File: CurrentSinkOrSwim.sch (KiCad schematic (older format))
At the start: 0 parts

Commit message: made a schematic
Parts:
- added C? (x3): C, ~, symbol C
- added P?: CONN_2, symbol CONN_2
- added Q?: BUK9575, ~, symbol MOSFET_N
- added R?: 0.1, ~, symbol R
- added R?: 27K, ~, symbol R
- added R?: 26.6K, ~, symbol R
- added R?: 0, ~, symbol R
- added R? (x2): R, ~, symbol R
- added U?: LM2931D-R, ~, symbol LM2931D-R
- added U? (x2): OP275, symbol OP275
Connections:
- net labels added: 2.7V, GND
- wire segments 0 -> 41

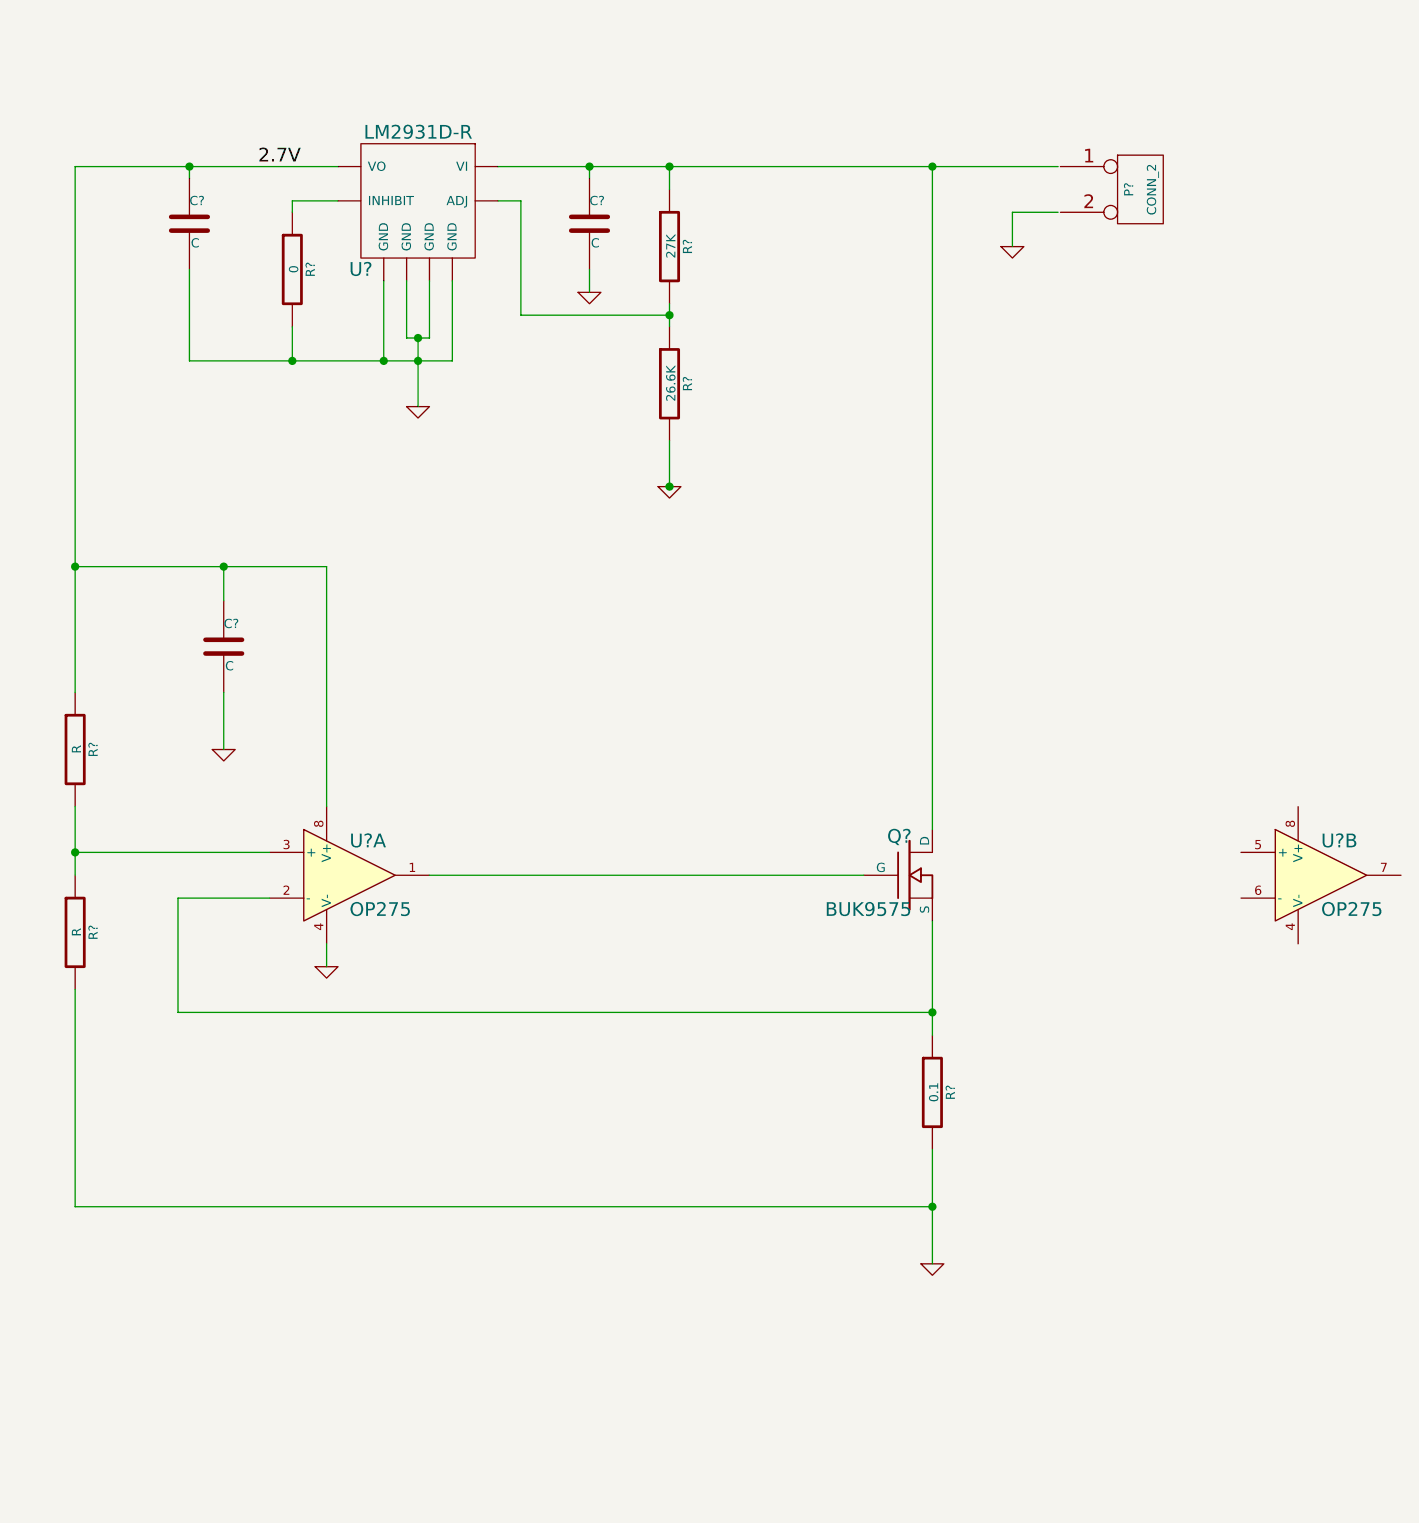
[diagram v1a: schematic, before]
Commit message: Updating the schematic
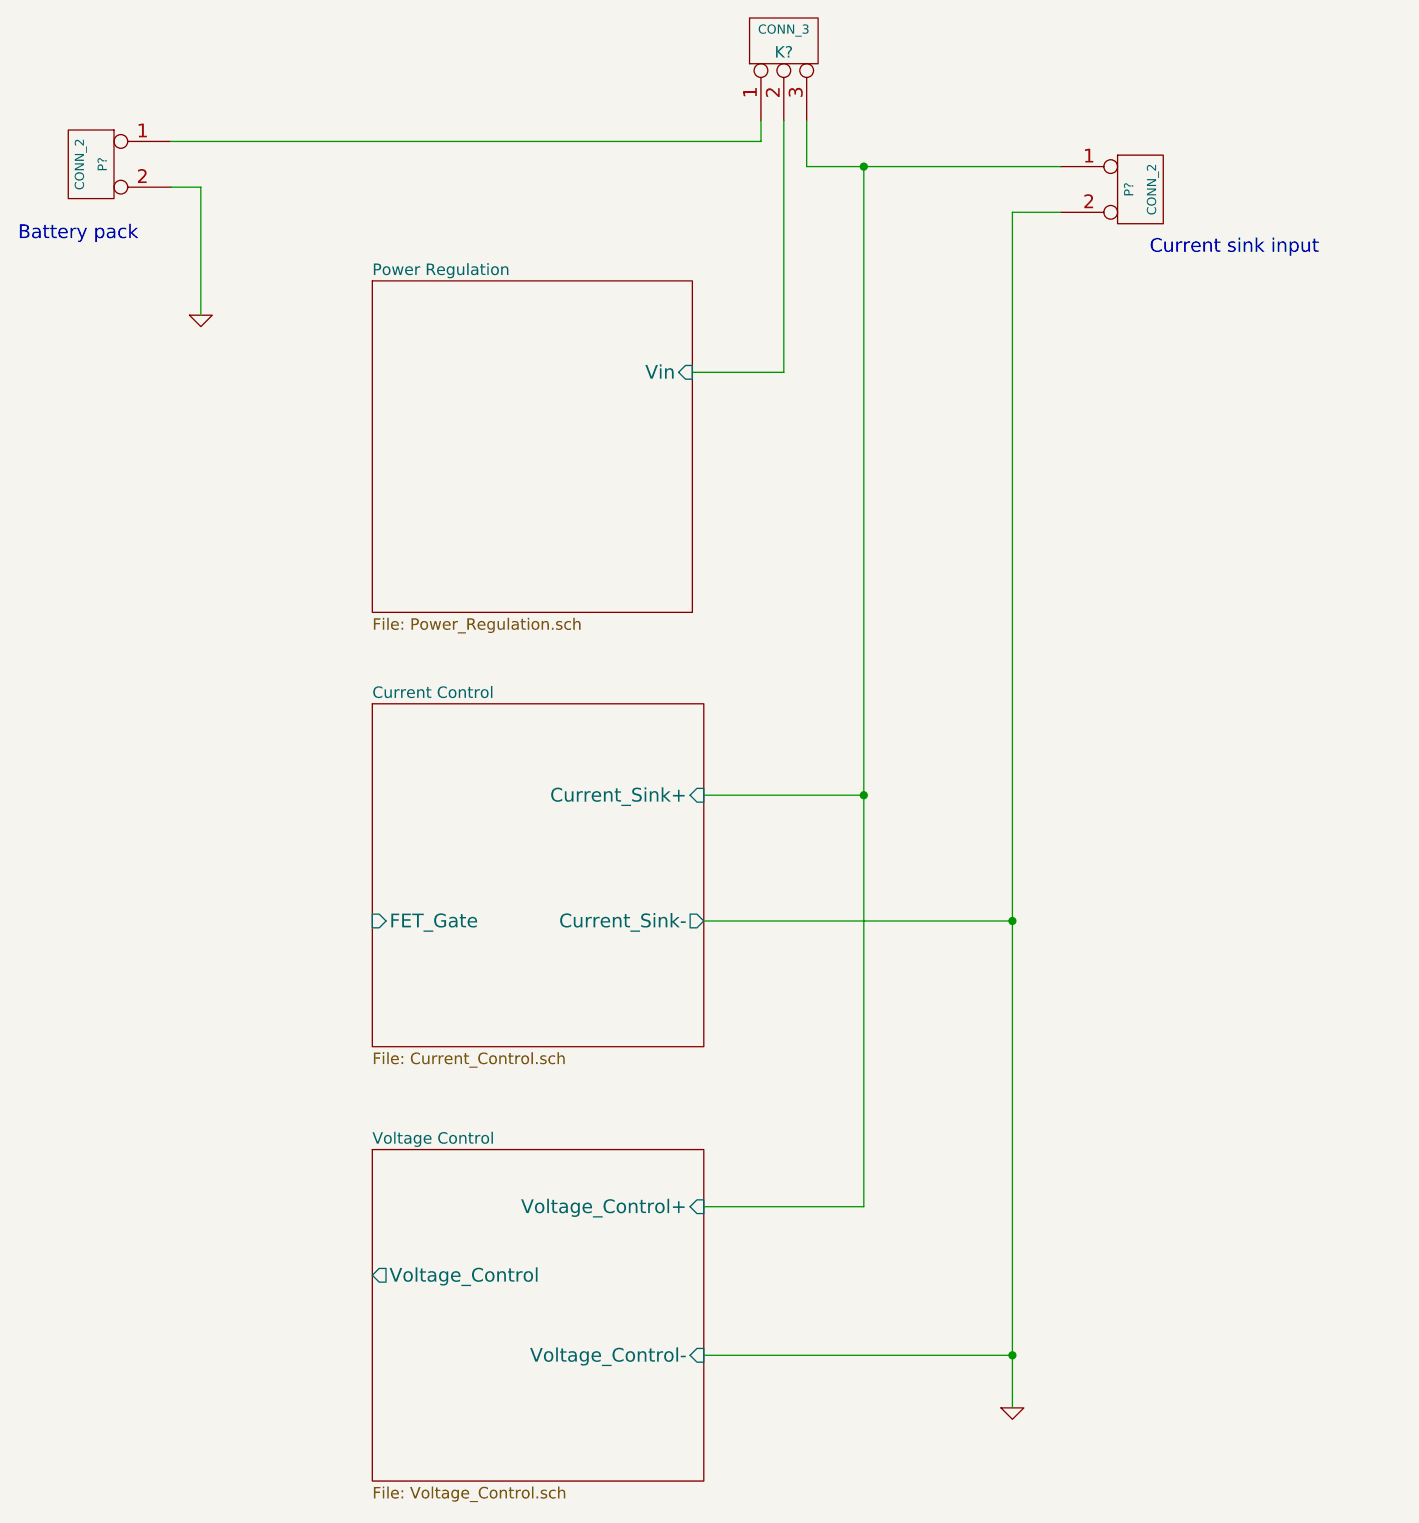
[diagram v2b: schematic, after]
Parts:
- removed C? (x3): C, ~, symbol C
- removed Q?: BUK9575, ~, symbol MOSFET_N
- removed R?: 0.1, ~, symbol R
- removed R?: 27K, ~, symbol R
- removed R?: 26.6K, ~, symbol R
- removed R?: 0, ~, symbol R
- removed R? (x2): R, ~, symbol R
- removed U?: LM2931D-R, ~, symbol LM2931D-R
- removed U? (x2): OP275, symbol OP275
- added K?: CONN_3, symbol CONN_3
- added P?: CONN_2, symbol CONN_2
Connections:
- net labels removed: 2.7V
- wire segments 41 -> 15
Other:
- note added: "Battery pack"
- note added: "Current sink input"
